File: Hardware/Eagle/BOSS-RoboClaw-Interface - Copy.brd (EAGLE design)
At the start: 41.6 x 48.3 mm, 9 parts, among them IC1 ISO7221ISO7221, J1 MOLEX 22112022, J2 MOLEX 22122034, J3 Amphenol 75869-130LF, J4 SAMTEC ESQ-105-44-G-S, J5 SAMTEC ESW-110-44-S-D, X1 Amphenol L77SDAH15SOL2RM8C309

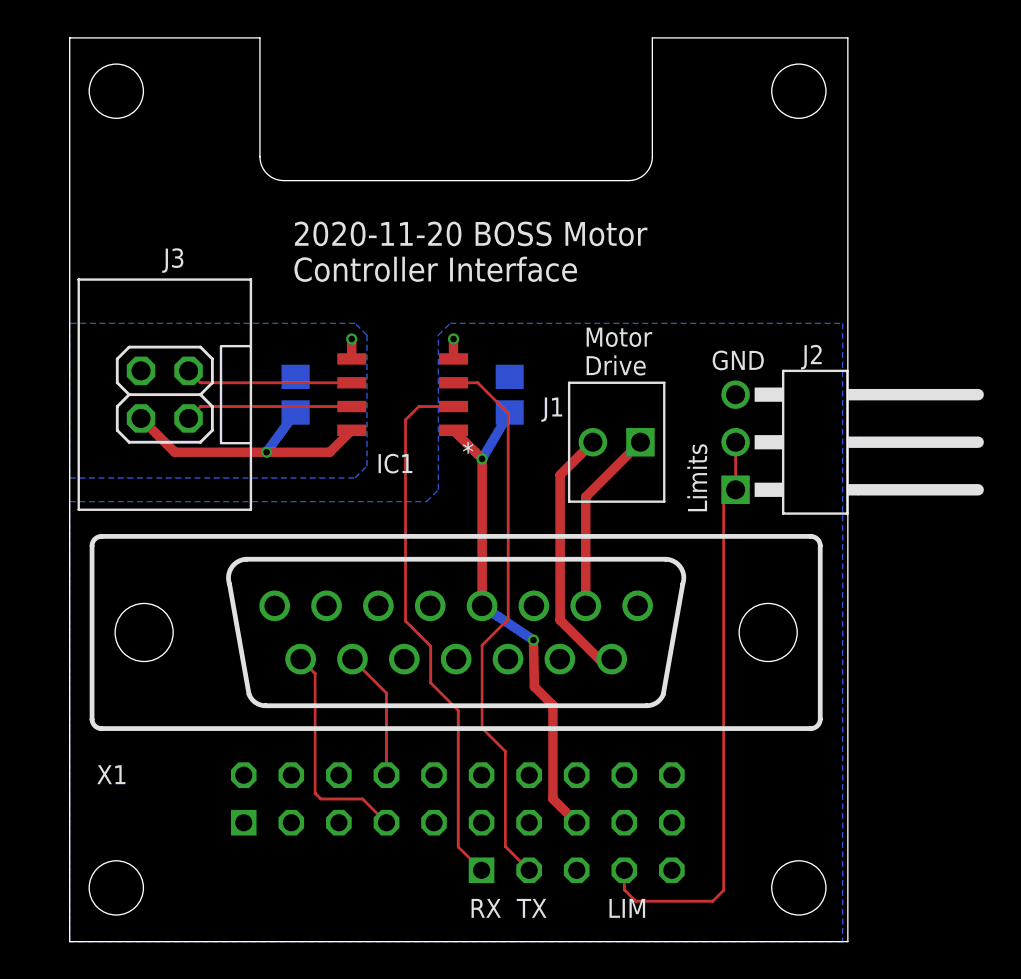
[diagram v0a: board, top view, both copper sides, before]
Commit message: Changed connectors and board outline to be able to use existing screw connectors
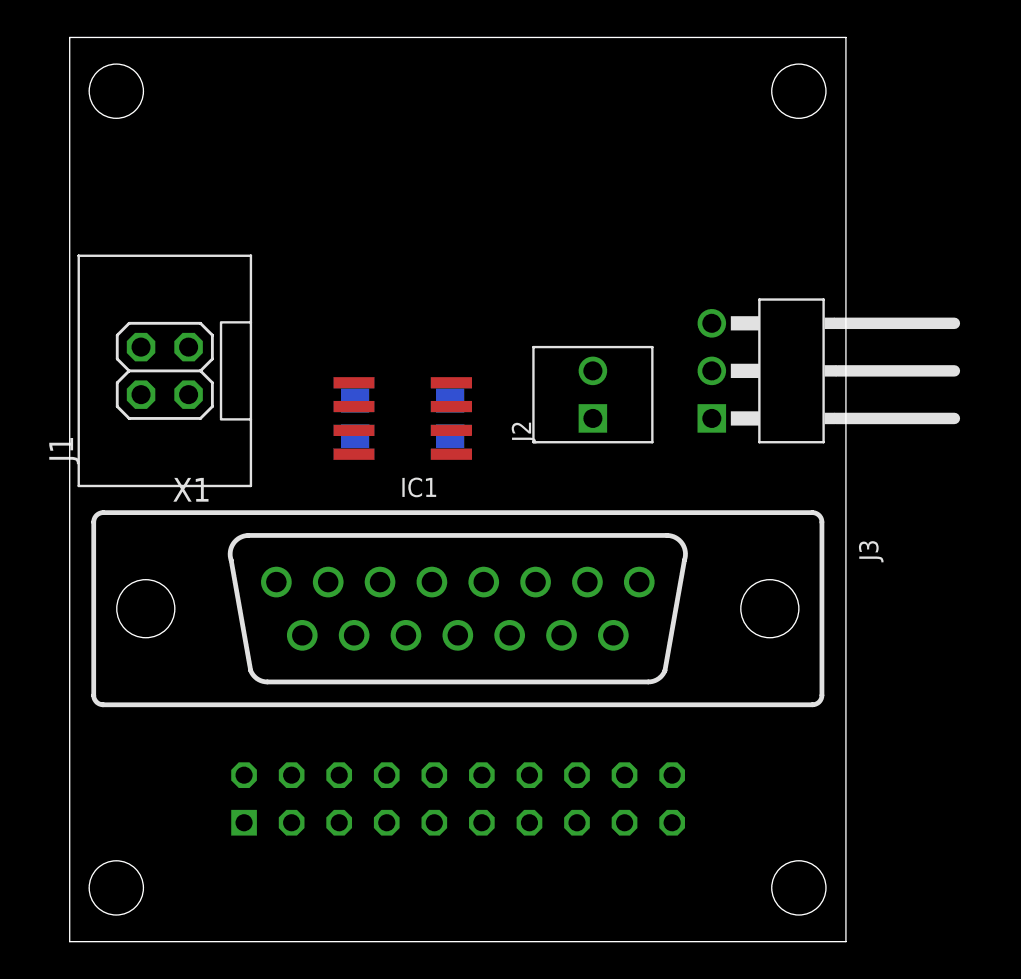
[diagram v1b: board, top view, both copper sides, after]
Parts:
- removed J5: SAMTEC ESW-110-44-S-D, AUmlib:FE10-2-SAMTEC-ESW-110-44-S-D
- IC1: value ISO7221ISO7221 -> ISO7221A; device AUmlib:SO-08-ISO7221 -> AUmlib:SO-08
- J1: value MOLEX 22112022 -> (none); device AUmlib:1X02-MOLEX-22112022 -> AUmlib:2X02-SHROUD
- J2: value MOLEX 22122034 -> PINHD-1X2-MOLEX-22112022; device AUmlib:1X03RA-MOLEX-22122034 -> AUmlib:1X02-MOLEX-22112022
- J3: value Amphenol 75869-130LF -> Molex 22122034; device AUmlib:2X02-SHROUD -> AUmlib:1X03RA-MOLEX-22122034
- J4: value SAMTEC ESQ-105-44-G-S -> (none); device AUmlib:FE05-1 -> AUmlib:FE10-2-SAMTEC-ESW-110-44-S-D
- moved J3 33.0 mm to (38.1, 30.5)
- moved J1 25.7 mm to (5.08, 30.5), turned to 90 degrees
- moved J2 11.5 mm to (27.9, 27.9)
- moved J4 7.39 mm to (20.7, 7.62)
- moved C1 3.42 mm to (20.3, 27.9)
- moved C2 3.42 mm to (15.2, 27.9)
- moved X1 1.27 mm to (20.7, 17.8)
- moved IC1 1.27 mm to (17.8, 27.9), turned to 90 degrees
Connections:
- removed net LIMIT: J2.1, J2.2, J4.4
- removed net RXMCU: IC1.6, J3.3
- removed net TXMCU: IC1.7, J3.1
- new net LIMIT/HOME: J3.1, J3.2
- new net N$1: IC1.7, J1.1
- new net N$2: IC1.6, J1.3
- net ENC1A: no longer J5.8
- net ENC1B: no longer J5.7
- net GND: now also J3.3; no longer J2.3, J5.16
- net GND-ISO: now also J1.4; no longer J3.4
- net M1A: now also J2.2, X1.9; no longer J1.1, X1.2
- net M1B: now also J2.1, X1.2; no longer J1.2, X1.9
- net RX: no longer J4.1
- net TX: no longer J4.2
- net VCC1: no longer J5.15
- net VCC2: now also J1.2; no longer J3.2
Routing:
- net LIMIT: track 31.0 -> 0.00 mm
- net TX: track 29.6 -> 0.00 mm
- net RX: track 28.6 -> 0.00 mm
- net VCC1: track 26.9 -> 0.00 mm, vias 2 -> 0
- net VCC2: track 15.1 -> 0.00 mm, vias 1 -> 0
- net M1B: track 13.8 -> 0.00 mm
- net ENC1B: track 11.9 -> 0.00 mm
- net M1A: track 9.95 -> 0.00 mm
- net RXMCU: track 8.98 -> 0.00 mm
- net TXMCU: track 8.98 -> 0.00 mm
- net ENC1A: track 6.95 -> 0.00 mm
- net GND-ISO: track 1.07 -> 0.00 mm, vias 1 -> 0
- net GND: track 1.07 -> 0.00 mm, vias 1 -> 0
- removed copper zone on layer 16, net GND
- removed copper zone on layer 16, net GND-ISO
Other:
- board size 41.6 x 48.3 mm -> 41.5 x 48.3 mm
- board text added: "2019-03-01 BOSS Spectrograph PI M-227.10 Motor to Basic Micro RoboClaw2x7A Controller"
- board text removed: "2020-11-20 BOSS Motor Controller Interface"
- board text removed: "GND"
- board text removed: "LIM"
- board text removed: "Limits"
- board text removed: "Motor Drive"
- board text removed: "RX"
- board text removed: "TX"
